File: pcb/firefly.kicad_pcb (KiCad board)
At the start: 4 copper layers, 85 x 57.5 mm, 105 parts, among them J1 RJ45_Shielded, J101 Conn_02x03_Counter_Clockwise, J2 RJ45_Shielded, J3 USB_B, SW101 SW_DIP_x08, SW102 RESET, U101 ATmega328PB-AU, U102 TLV75733PDBV, U103 ADM2687E, U104 AMS1117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

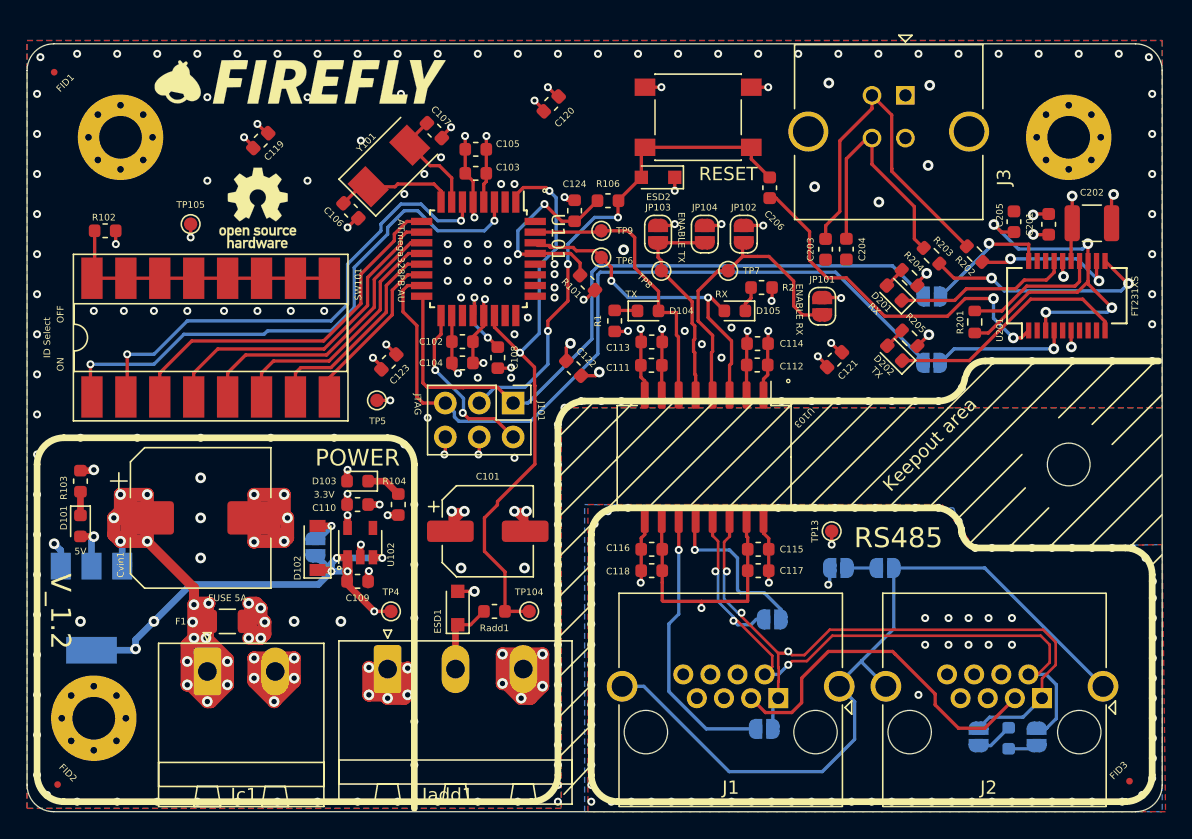
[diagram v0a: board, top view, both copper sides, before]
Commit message: Adding logos, fixing text
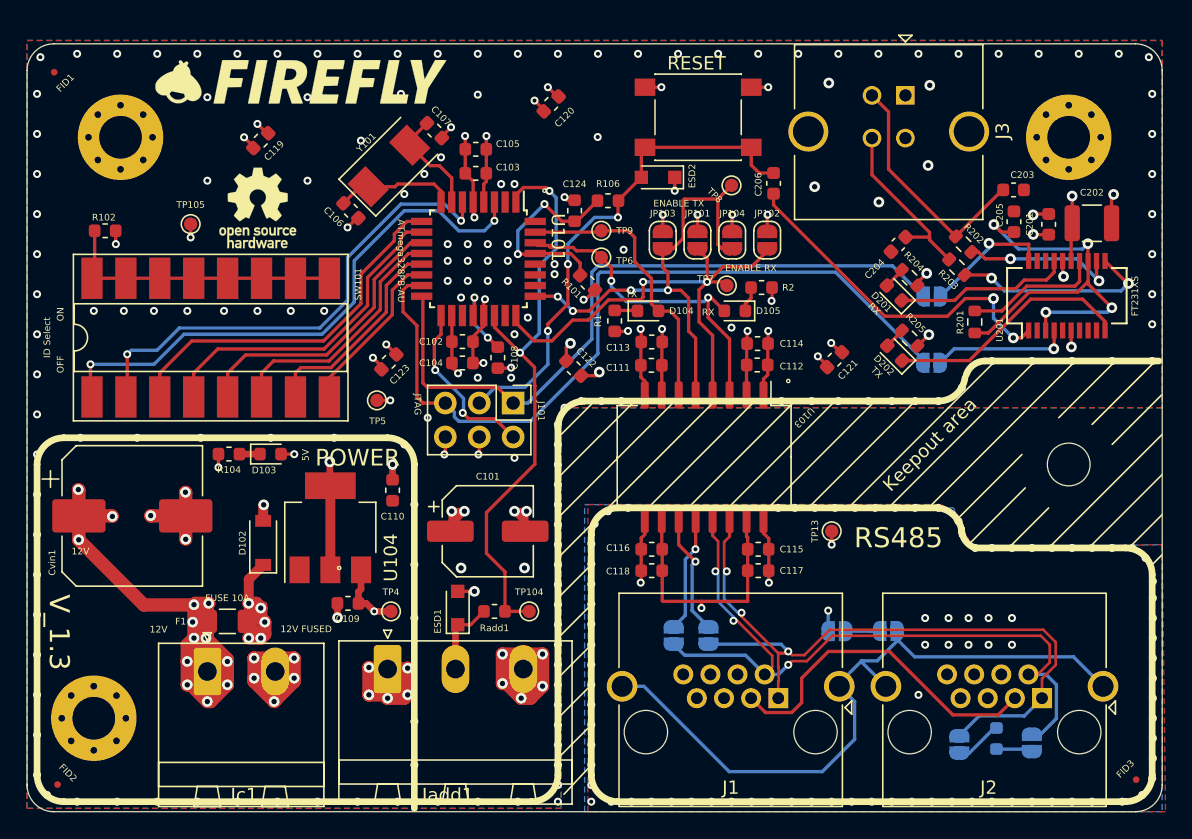
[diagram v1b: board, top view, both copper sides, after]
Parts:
- removed D101: LED_5V, LED_SMD:LED_0603_1608Metric
- removed the G*** at (156.6, 61.4)
- removed the G*** at (154.1, 75.3)
- removed the G*** at (183.3, 73.5)
- removed JP109: Jumper, Jumper:SolderJumper-2_P1.3mm_Open_RoundedPad1.0x1.5mm
- removed R103: 300, Resistor_SMD:R_0603_1608Metric
- removed the REF** at (166.4, 73.3)
- removed U102: TLV75733PDBV, Package_TO_SOT_SMD:SOT-23-5
- added G***: LOGO, logo:FireFly_big, F.Cu at (156.7, 61.4)
- added G***: LOGO, logo:novena, B.Cu at (186.2, 70.4)
- added G***: LOGO, logo:radiona-16mm, B.Cu at (148.2, 71.1)
- added REF**: KiCad-Logo2_6mm_SilkScreen, Symbol:KiCad-Logo2_6mm_SilkScreen, B.Cu at (167.6, 94.6)
- U104: moved to F.Cu
- moved U104 18.9 mm to (158.8, 94.7), turned to 90 degrees
- moved C203 14.8 mm to (209.9, 69.4), turned to 0 degrees
- moved R104 13.2 mm to (151.2, 89.2), turned to 0 degrees
- moved JP101 10.6 mm to (186.3, 73.2)
- moved TP8 8.28 mm to (188.8, 69.1)
- moved JP106 8.14 mm to (187.1, 102.8), turned to 270 degrees
- moved JP105 7.48 mm to (184.5, 102.8), turned to 270 degrees
- moved D103 6.83 mm to (154.3, 89.2), turned to 0 degrees
- moved Cvin1 5.12 mm to (144.0, 93.8)
- moved JP107 4.73 mm to (196.7, 102.5)
- moved JP108 4.73 mm to (200.6, 102.5)
- moved D102 4.09 mm to (153.8, 95.9)
- moved C204 3.91 mm to (201.3, 73.5), turned to 225 degrees
- moved C110 2.83 mm to (163.4, 91.9), turned to 270 degrees
- moved JP104 2.10 mm to (188.9, 73.2)
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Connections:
- C109 pad 1: +5V -> Vin_fused
- D102 pad 1: +5V -> Vin_fused
- TP4 pad 1: +5V -> Vin_fused
- U101 pad 24: (no net) -> /DMX_Enable_Receive
- U101 pad 25: (no net) -> /DMX_Enable_Send
- U104 pad 2: +5V -> +3V3
- U104 pad 3: /Vin -> Vin_fused
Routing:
- net +5V: track 40.4 -> 0.00 mm, vias 8 -> 0
- net /DMX_Enable_Send: track 16.3 -> 37.0 mm, vias 0 -> 4
- net GND1: track 125.1 -> 106.4 mm, vias 227 -> 212
- net /DMX_Enable_Receive: track 23.5 -> 37.1 mm, vias 0 -> 2
- net +3V3: track 50.8 -> 63.2 mm
- net /RS485_transciever/DMXTransmitterY: track 20.9 -> 9.19 mm
- net /Vin: track 77.3 -> 66.8 mm, vias 15 -> 13
- net Vin_fused: track 28.9 -> 38.2 mm, vias 10 -> 11
- net Net-(C203-Pad1): track 26.5 -> 18.2 mm
- net /RS485_transciever/DMX+: track 51.1 -> 57.0 mm
- net /RS485_transciever/DMXchassignd: track 58.1 -> 52.3 mm
- net /RS485_transciever/DMX-: track 49.4 -> 55.2 mm
- net Net-(C204-Pad1): track 18.4 -> 13.7 mm
- net /RS485_transciever/DMXTransmitterZ: track 12.8 -> 8.74 mm
- net Net-(R203-Pad1): track 17.7 -> 15.4 mm
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- added copper zone on POWER.Cu, net /Vin
- removed copper zone on POWER.Cu, net +5V
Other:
- board text added: "12V"
- board text added: "12V FUSED"
- board text added: "12V/DC IN"
- board text added: "12V_OUT"
- board text added: "FUSE 10A"
- board text added: "V_1.3"
- board text removed: "3.3V"
- board text removed: "5V/DC IN"
- board text removed: "5V_OUT"
- board text removed: "FUSE 5A"
- board text removed: "V_1.2"

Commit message: Before production export changes
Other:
- rule pad_to_mask_clearance: 0.05 -> 0

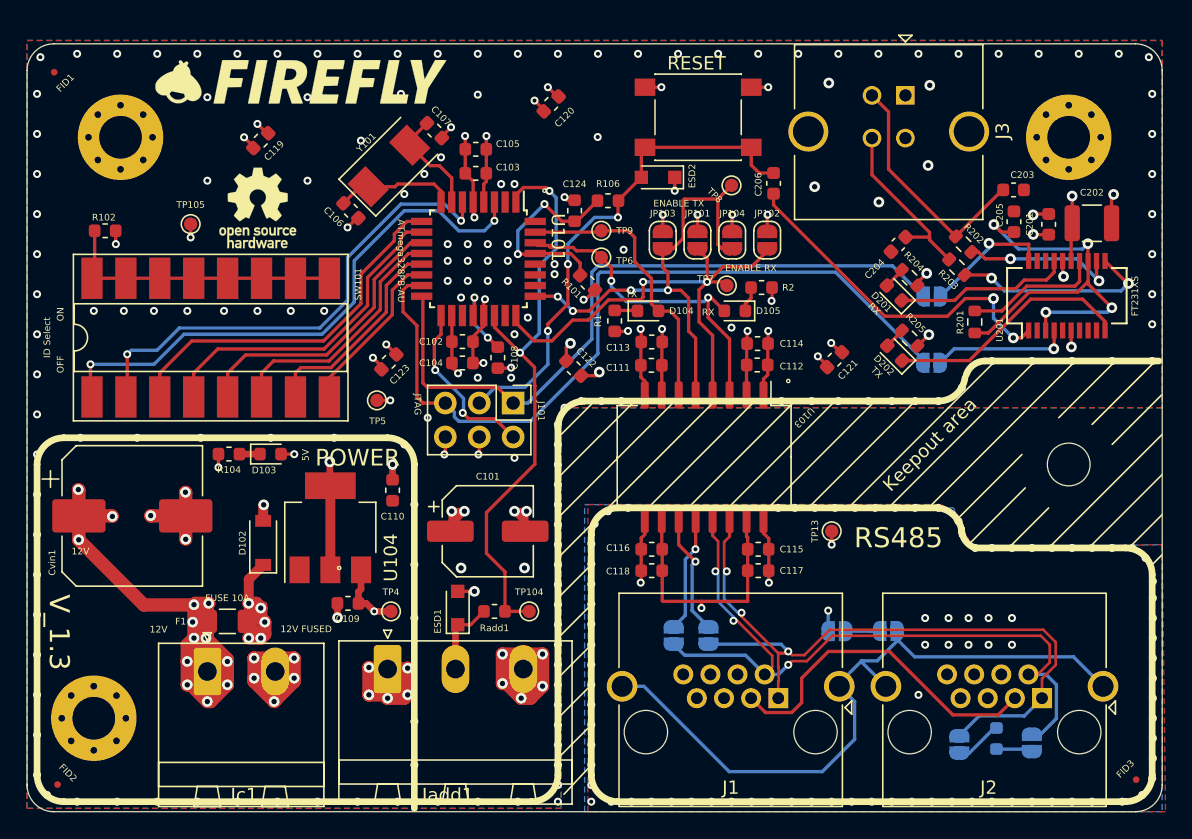
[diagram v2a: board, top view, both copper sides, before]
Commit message: Adding protection diodes
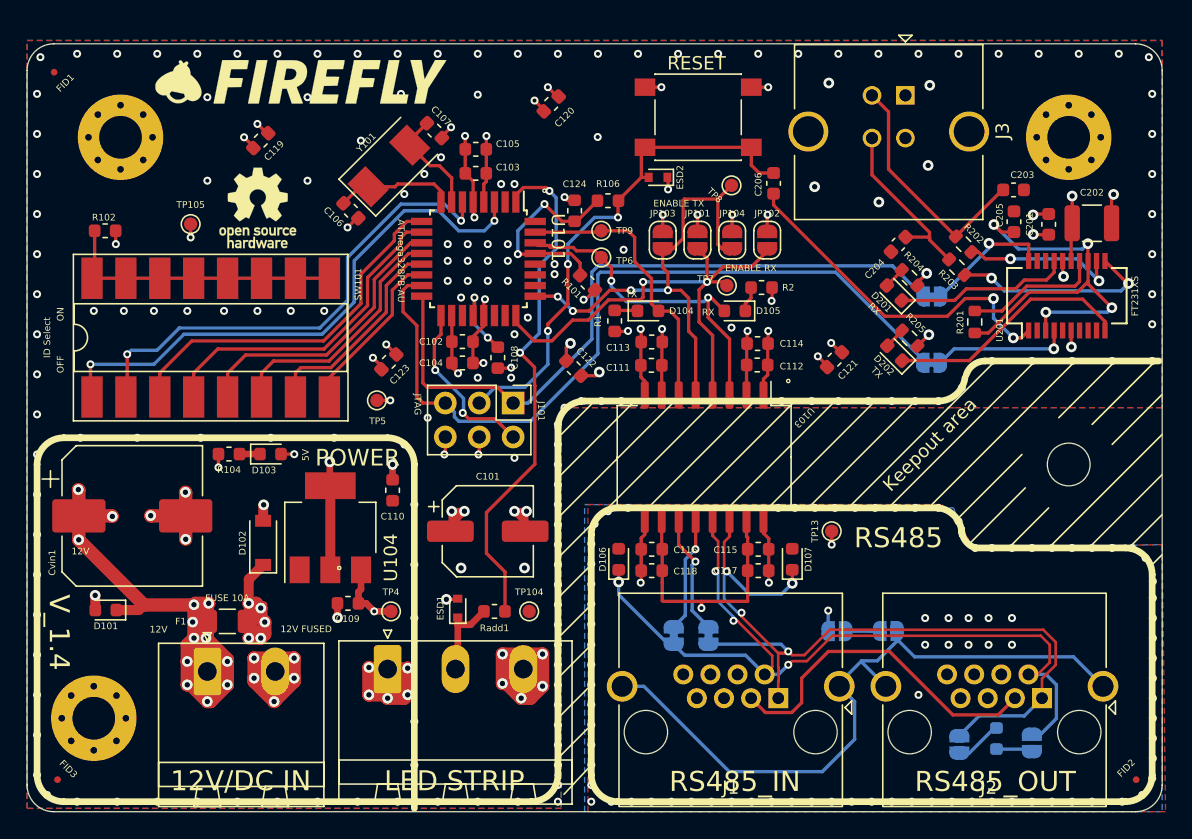
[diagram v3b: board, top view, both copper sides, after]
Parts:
- removed the REF** at (167.6, 94.6)
- added D101: 82306120029, Diode_SMD:D_0603_1608Metric, F.Cu at (142.0, 100.9)
- added D106: 82306120029, Diode_SMD:D_0603_1608Metric, F.Cu at (180.4, 97.1)
- added D107: 82306120029, Diode_SMD:D_0603_1608Metric, F.Cu at (193.4, 97.1)
- added REF**: KiCad-Logo2_8mm_SilkScreen, Symbol:KiCad-Logo2_8mm_SilkScreen, B.Cu at (164.8, 96.8)
- ESD1, ESD2: footprint Diode_SMD:D_SOD-323_HandSoldering -> Diode_SMD:D_SOD-523
- JP105, JP106, JP3, JP4: footprint Jumper:SolderJumper-2_P1.3mm_Open_RoundedPad1.0x1.5mm -> Jumper:SolderJumper-2_P1.3mm_Bridged_RoundedPad1.0x1.5mm
- moved FID2 80.8 mm to (219.1, 113.6)
- moved FID3 80.8 mm to (138.4, 113.6)
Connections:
- TP104 pad 1: /Addressable -> (no net)
- U101 pad 22: /Addressable -> (no net)
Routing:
- net /RS485_transciever/DMX-: track 55.2 -> 62.7 mm, vias 3 -> 4
- net /RS485_transciever/DMX+: track 57.0 -> 64.0 mm, vias 3 -> 4
- net /Addressable: track 44.1 -> 38.7 mm
- net /Vin: track 66.8 -> 69.1 mm
- net /RST: track 38.4 -> 38.9 mm
- net Net-(ESD1-Pad1): track 5.77 -> 6.32 mm
- net GND1: track 106.4 -> 106.6 mm, vias 212 -> 213
- added copper zone on POWER.Cu, net GND2
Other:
- board text added: "V_1.4"
- board text removed: "V_1.3"

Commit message: Changing USB connector - rerouting
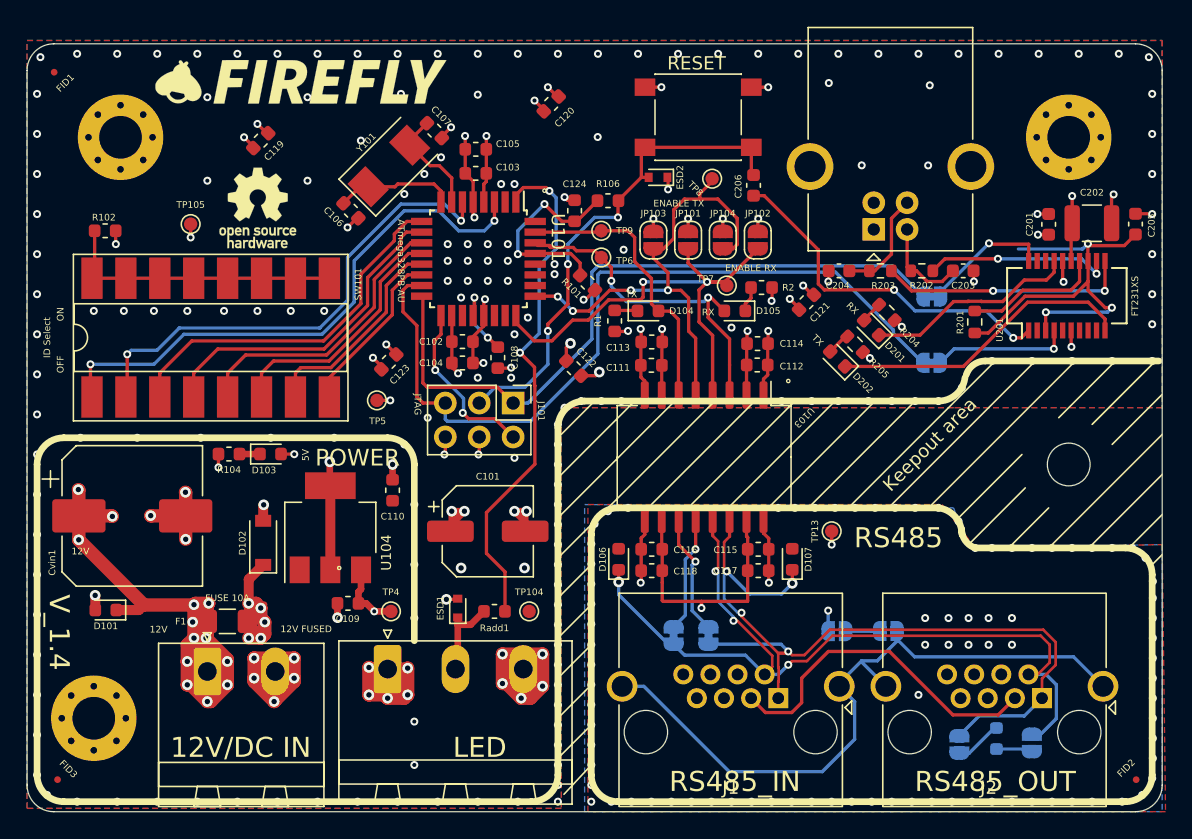
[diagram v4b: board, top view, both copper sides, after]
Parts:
- removed the REF** at (140.9, 90.6)
- removed the REF** at (140.9, 83.2)
- J3: footprint Connector_USB:USB_B_TE_5787834_Vertical -> Connector_USB:USB_B_OST_USB-B1HSxx_Horizontal
- moved J3 10.3 mm to (199.5, 72.4), turned to 90 degrees
- moved C205 9.10 mm to (219.1, 72.0)
- moved G*** 8.38 mm to (183.8, 78.4)
- moved C203 7.14 mm to (206.2, 75.5)
- moved R203 5.74 mm to (200.0, 75.5), turned to 180 degrees
- moved C204 4.86 mm to (196.9, 75.5), turned to 180 degrees
- moved C121 4.79 mm to (194.4, 77.9)
- moved D202 4.30 mm to (196.8, 82.1)
- moved R205 4.11 mm to (198.1, 81.0)
- moved R202 3.71 mm to (203.1, 75.5), turned to 180 degrees
- moved R204 3.11 mm to (200.5, 78.6)
- moved D201 3.11 mm to (199.3, 79.8)
- moved TP8 1.53 mm to (187.4, 68.6)
- moved C206 1.51 mm to (190.5, 69.1)
- moved JP101 0.70 mm to (185.6, 73.2)
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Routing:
- net Net-(C203-Pad1): track 18.2 -> 7.03 mm
- net Net-(C204-Pad1): track 13.7 -> 8.00 mm
- net Net-(D202-Pad1): track 18.5 -> 22.8 mm
- net Net-(R203-Pad1): track 15.4 -> 18.8 mm
- net Net-(D201-Pad1): track 13.1 -> 15.9 mm
- net GND1: track 106.6 -> 108.8 mm, vias 213 -> 214
- net +3V3: track 63.2 -> 61.2 mm
- net Net-(R202-Pad1): track 12.0 -> 14.1 mm
- net /DMX_Enable_Send: track 37.0 -> 38.6 mm
- net /RST: track 38.9 -> 37.8 mm
- net Net-(C205-Pad2): track 31.8 -> 31.7 mm, vias 4 -> 3
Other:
- board text added: "LED"

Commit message: Adding two connectors with 4 analog inputs
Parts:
- added J102: Analog_1_2, Connector_PinHeader_1.00mm:PinHeader_2x03_P1.00mm_Vertical, F.Cu at (173.5, 61.4)
- added J103: Analog_3_4, Connector_PinHeader_1.00mm:PinHeader_2x03_P1.00mm_Vertical, F.Cu at (176.9, 61.4)
- moved C120 3.47 mm to (176.0, 66.4)
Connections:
- U101 pad 23: (no net) -> /A0
- U101 pad 26: (no net) -> /A3
- U101 pad 27: (no net) -> /A4
- U101 pad 28: (no net) -> /A5
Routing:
- net /A3: track 0.00 -> 18.1 mm, vias 0 -> 1
- net /A5: track 0.00 -> 17.8 mm, vias 0 -> 1
- net /A0: track 0.00 -> 17.5 mm, vias 0 -> 1
- net /A4: track 0.00 -> 17.1 mm, vias 0 -> 1
- net /Addressable: track 38.7 -> 34.6 mm
- net GND1: track 108.8 -> 106.0 mm, vias 214 -> 208
- net Net-(C124-Pad1): track 15.6 -> 17.7 mm
- net /DMX_Receive: track 25.4 -> 26.1 mm
- net /RST: track 37.8 -> 37.3 mm
